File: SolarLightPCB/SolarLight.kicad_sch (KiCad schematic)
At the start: 18 parts, among them J1 I2C, J2 SPI, SW1 RotaryEncoder_Switch, U1 TP4056, U2 WeMos_D1_mini, U3 MCP1700-3302E

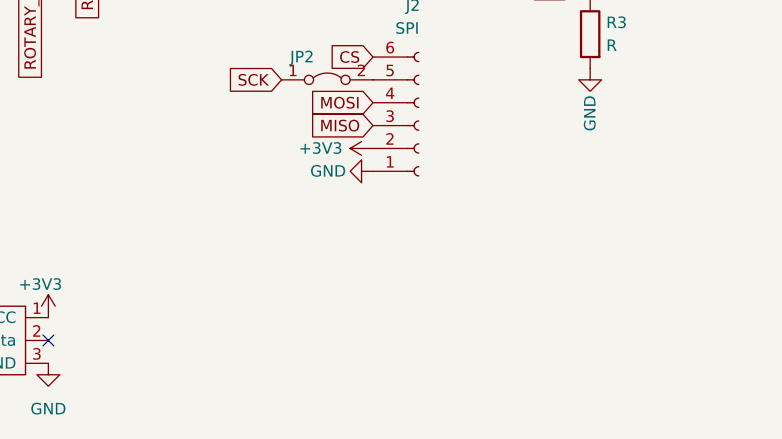
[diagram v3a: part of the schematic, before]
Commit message: Add GND Jumper
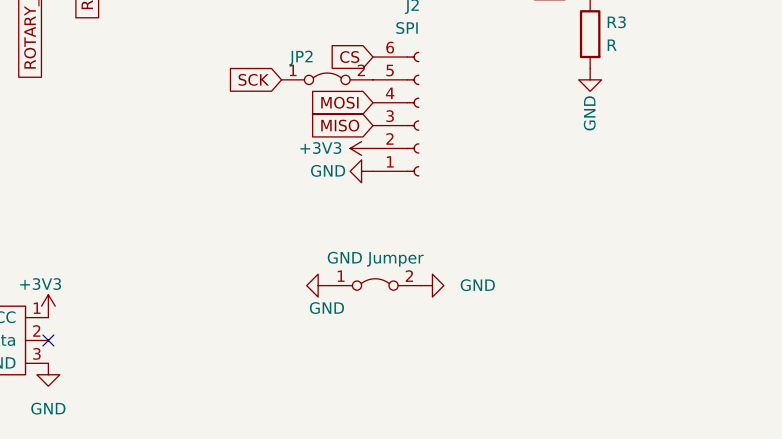
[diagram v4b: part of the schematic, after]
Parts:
- added JP6: GND Jumper, Resistor_THT:R_Axial_DIN0204_L3.6mm_D1.6mm_P5.08mm_Horizontal, symbol Jumper:Jumper_2_Bridged
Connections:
- net GND: now also JP6.1 (A), JP6.2 (B)
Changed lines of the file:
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@@
+    (pin "1")
+  )
+  (symbol (lib_id "power:GND") (at 185.42 130.048 270) (unit 1)
+    (in_bom yes) (on_board yes)
+    (property "Reference" "#PWR0121" (id 0) (at 179.07 130.048 0)
+      (effects (font (size 1.27 1.27)) hide)
+    )
+    (property "Value" "GND" (id 1) (at 183.134 132.588 90)
+      (effects (font (size 1.27 1.27)) (justify left))
+    )
+    (property "Footprint" "" (id 2) (at 185.42 130.048 0)
+      (effects (font (size 1.27 1.27)) hide)
+    )
+    (property "Datasheet" "" (id 3) (at 185.42 130.048 0)
+      (effects (font (size 1.27 1.27)) hide)
+    )
     (pin "1")
   )
@@
     (pin "6")
   )
+  (symbol (lib_id "Jumper:Jumper_2_Bridged") (at 190.5 130.048 0) (unit 1)
+    (in_bom yes) (on_board yes)
+    (property "Reference" "JP6" (id 0) (at 190.5 128.016 0)
+      (effects (font (size 1.27 1.27)) hide)
+    )
+    (property "Value" "GND Jumper" (id 1) (at 190.5 127 0))
+    (property "Footprint" "Resistor_THT:R_Axial_DIN0204_L3.6mm_D1.6mm_P5.08mm_Horizontal" (id 2) (at 190.5 130.048 0)
+      (effects (font (size 1.27 1.27)) hide)
+    )
+    (property "Datasheet" "~" (id 3) (at 190.5 130.048 0)
+      (effects (font (size 1.27 1.27)) hide)
+    )
+    (pin "1")
+    (pin "2")
+  )
   (symbol (lib_id "Jumper:SolderJumper_3_Bridged12") (at 152.146 90.424 270) (unit 1)
     (in_bom yes) (on_board yes) (fields_autoplaced)
@@
     )
     (property "Datasheet" "" (id 3) (at 197.866 63.246 0)
+      (effects (font (size 1.27 1.27)) hide)
+    )
+    (pin "1")
+  )
+  (symbol (lib_id "power:GND") (at 195.58 130.048 90) (unit 1)
+    (in_bom yes) (on_board yes) (fields_autoplaced)
+    (property "Reference" "#PWR0120" (id 0) (at 201.93 130.048 0)
+      (effects (font (size 1.27 1.27)) hide)
+    )
+    (property "Value" "GND" (id 1) (at 199.898 130.0479 90)
+      (effects (font (size 1.27 1.27)) (justify right))
+    )
+    (property "Footprint" "" (id 2) (at 195.58 130.048 0)
+      (effects (font (size 1.27 1.27)) hide)
+    )
+    (property "Datasheet" "" (id 3) (at 195.58 130.048 0)
       (effects (font (size 1.27 1.27)) hide)
     )
@@
       (reference "#PWR0119") (unit 1) (value "+3V3") (footprint "")
     )
+    (path "/8f53287b-acc6-4dbe-ac6e-98fe51c515c9"
+      (reference "#PWR0120") (unit 1) (value "GND") (footprint "")
+    )
+    (path "/053f9927-e4f2-4987-bb2c-996f494ab85a"
+      (reference "#PWR0121") (unit 1) (value "GND") (footprint "")
+    )
     (path "/1b639698-fdc2-412d-93eb-4fc53c894eea"
       (reference "BT1") (unit 1) (value "Battery_Cell") (footprint "Connector_PinHeader_2.54mm:PinHeader_1x02_P2.54mm_Vertical")
@@
       (reference "JP5") (unit 1) (value "POWER ON") (footprint "Connector_PinHeader_2.54mm:PinHeader_1x02_P2.54mm_Vertical")
     )
+    (path "/8628d11f-5b21-4013-8421-97343e641f3e"
+      (reference "JP6") (unit 1) (value "GND Jumper") (footprint "Resistor_THT:R_Axial_DIN0204_L3.6mm_D1.6mm_P5.08mm_Horizontal")
+    )
     (path "/efe1edb9-34c9-473f-839b-20e06ddf294c"

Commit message: Make a “simplified” version
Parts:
- removed J2: SPI, Connector_PinHeader_2.54mm:PinHeader_1x06_P2.54mm_Vertical, symbol Connector:Conn_01x06_Female
- removed JP1: Deep Sleep, Jumper:SolderJumper-2_P1.3mm_Bridged_Pad1.0x1.5mm, symbol Jumper:SolderJumper_2_Bridged
- removed JP2: Jumper_2_Bridged, Resistor_THT:R_Axial_DIN0204_L3.6mm_D1.6mm_P5.08mm_Horizontal, symbol Jumper:Jumper_2_Bridged
- removed JP3, JP4: SolderJumper_3_Bridged12, Jumper:SolderJumper-3_P1.3mm_Bridged12_Pad1.0x1.5mm, symbol Jumper:SolderJumper_3_Bridged12
- removed JP5: POWER ON, Connector_PinHeader_2.54mm:PinHeader_1x02_P2.54mm_Vertical, symbol Jumper:Jumper_2_Bridged
- removed JP6: GND Jumper, Resistor_THT:R_Axial_DIN0204_L3.6mm_D1.6mm_P5.08mm_Horizontal, symbol Jumper:Jumper_2_Bridged
- removed SW1: RotaryEncoder_Switch, Rotary_Encoder:RotaryEncoder_Alps_EC12E-Switch_Vertical_H20mm, symbol Device:RotaryEncoder_Switch
- added J2: Conn_01x06_Male, Connector_PinHeader_2.54mm:PinHeader_1x06_P2.54mm_Vertical, symbol Connector:Conn_01x06_Male
- added SW1: SW_Push, Button_Switch_THT:SW_PUSH_6mm_H4.3mm, symbol Switch:SW_Push
- BT1, SC1: footprint Connector_PinHeader_2.54mm:PinHeader_1x02_P2.54mm_Vertical -> TerminalBlock_Phoenix:TerminalBlock_Phoenix_PT-1,5-2-3.5-H_1x02_P3.50mm_Horizontal
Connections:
- net +3V3: now also J1.3 (Pin_3), U3.3 (VO), J2.2 (Pin_2); no longer J1.1 (Pin_1)
- net CS: now also J2.6 (Pin_6)
- net GND: now also J2.1 (Pin_1), SW1.2
- net MISO: now also J2.4 (Pin_4)
- net MOSI: now also J2.3 (Pin_3)
- net ROTARY_SWITCH: now also SW1.1
- net RST: now also U2.3 (D0)
- net SCK: now also J2.5 (Pin_5)
- net SCL: now also J1.1 (Pin_1), U2.14 (SCL/D1); no longer J1.2 (Pin_2)
- net SDA: now also J1.2 (Pin_2), U2.13 (SDA/D2); no longer J1.3 (Pin_3)
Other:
- moved on the sheet: BT1, J1, LIN1, LOUT1, U1, U2, U3

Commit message: Updated the simple pcb
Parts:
- added SW2: ON_OFF, Connector_PinHeader_2.54mm:PinHeader_1x03_P2.54mm_Vertical, symbol Switch:SW_SPST
- C1: footprint Capacitor_THT:CP_Radial_D5.0mm_P2.00mm -> Capacitor_THT:CP_Radial_D5.0mm_P2.50mm
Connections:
- net +3V3: now also SW2.2 (B); no longer LIN1.1 (VCC), LOUT1.1 (VCC), U3.3 (VO)
- net SCL: now also J1.2 (Pin_2); no longer J1.1 (Pin_1)
- net SDA: now also J1.1 (Pin_1); no longer J1.2 (Pin_2)
- net VOUT: now reaches U1.3 (OUT+), U3.2 (VI)
- net VOUT: now also LIN1.1 (VCC)
- new net: SW2.1 (A), U3.3 (VO)
- no-connect marks 4 -> 5
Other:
- moved on the sheet: C1
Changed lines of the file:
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@@
   )
   (no_connect (at 109.728 103.124))
+  (no_connect (at 83.312 100.584))
   (no_connect (at 153.67 96.52))
   (no_connect (at 146.05 114.3))
@@
     (stroke (width 0) (type default) (color 0 0 0 0))
   )
-  (global_label "SCL" (shape input) (at 190.5 77.47 180) (fields_autoplaced)
-    (effects (font (size 1.27 1.27)) (justify right))
-    (property "Intersheet References" "${INTERSHEET_REFS}" (id 0) (at 184.5793 77.3906 0)
+  (label "VOUT" (at 155.448 38.1 0)
+    (effects (font (size 1.27 1.27)) (justify left bottom))
+  )
+  (label "VOUT" (at 109.728 100.584 0)
+    (effects (font (size 1.27 1.27)) (justify left bottom))
+  )
+  (global_label "SCL" (shape input) (at 190.5 80.01 180) (fields_autoplaced)
+    (effects (font (size 1.27 1.27)) (justify right))
+    (property "Intersheet References" "${INTERSHEET_REFS}" (id 0) (at 184.5793 79.9306 0)
       (effects (font (size 1.27 1.27)) (justify right) hide)
     )
@@
     )
   )
-  (global_label "SDA" (shape input) (at 190.5 80.01 180) (fields_autoplaced)
-    (effects (font (size 1.27 1.27)) (justify right))
-    (property "Intersheet References" "${INTERSHEET_REFS}" (id 0) (at 184.5188 79.9306 0)
+  (global_label "SDA" (shape input) (at 190.5 77.47 180) (fields_autoplaced)
+    (effects (font (size 1.27 1.27)) (justify right))
+    (property "Intersheet References" "${INTERSHEET_REFS}" (id 0) (at 184.5188 77.3906 0)
       (effects (font (size 1.27 1.27)) (justify right) hide)
     )
@@
     (pin "1")
   )
-  (symbol (lib_id "power:+3V3") (at 109.728 100.584 0) (unit 1)
-    (in_bom yes) (on_board yes)
-    (property "Reference" "#PWR0106" (id 0) (at 109.728 104.394 0)
-      (effects (font (size 1.27 1.27)) hide)
-    )
-    (property "Value" "+3V3" (id 1) (at 108.839 96.901 0))
-    (property "Footprint" "" (id 2) (at 109.728 100.584 0)
-      (effects (font (size 1.27 1.27)) hide)
-    )
-    (property "Datasheet" "" (id 3) (at 109.728 100.584 0)
-      (effects (font (size 1.27 1.27)) hide)
-    )
-    (pin "1")
-  )
-  (symbol (lib_id "power:GND") (at 193.04 46.99 0) (unit 1)
-    (in_bom yes) (on_board yes) (fields_autoplaced)
-    (property "Reference" "#PWR0103" (id 0) (at 193.04 53.34 0)
-      (effects (font (size 1.27 1.27)) hide)
-    )
-    (property "Value" "GND" (id 1) (at 193.04 52.07 0))
-    (property "Footprint" "" (id 2) (at 193.04 46.99 0)
-      (effects (font (size 1.27 1.27)) hide)
-    )
-    (property "Datasheet" "" (id 3) (at 193.04 46.99 0)
+  (symbol (lib_id "power:GND") (at 199.898 44.958 0) (unit 1)
+    (in_bom yes) (on_board yes) (fields_autoplaced)
+    (property "Reference" "#PWR0103" (id 0) (at 199.898 51.308 0)
+      (effects (font (size 1.27 1.27)) hide)
+    )
+    (property "Value" "GND" (id 1) (at 199.898 50.038 0))
+    (property "Footprint" "" (id 2) (at 199.898 44.958 0)
+      (effects (font (size 1.27 1.27)) hide)
+    )
+    (property "Datasheet" "" (id 3) (at 199.898 44.958 0)
       (effects (font (size 1.27 1.27)) hide)
     )
@@
     (pin "1")
   )
-  (symbol (lib_id "power:+3V3") (at 179.07 38.1 0) (unit 1)
-    (in_bom yes) (on_board yes)
-    (property "Reference" "#PWR0104" (id 0) (at 179.07 41.91 0)
-      (effects (font (size 1.27 1.27)) hide)
-    )
-    (property "Value" "+3V3" (id 1) (at 179.578 32.258 0))
-    (property "Footprint" "" (id 2) (at 179.07 38.1 0)
-      (effects (font (size 1.27 1.27)) hide)
-    )
-    (property "Datasheet" "" (id 3) (at 179.07 38.1 0)
+  (symbol (lib_id "power:+3V3") (at 189.23 38.1 0) (unit 1)
+    (in_bom yes) (on_board yes)
+    (property "Reference" "#PWR0104" (id 0) (at 189.23 41.91 0)
+      (effects (font (size 1.27 1.27)) hide)
+    )
+    (property "Value" "+3V3" (id 1) (at 189.738 32.258 0))
+    (property "Footprint" "" (id 2) (at 189.23 38.1 0)
+      (effects (font (size 1.27 1.27)) hide)
+    )
+    (property "Datasheet" "" (id 3) (at 189.23 38.1 0)
       (effects (font (size 1.27 1.27)) hide)
     )
@@
     (pin "1")
   )
-  (symbol (lib_id "power:+3V3") (at 193.04 39.37 0) (unit 1)
-    (in_bom yes) (on_board yes) (fields_autoplaced)
-    (property "Reference" "#PWR0105" (id 0) (at 193.04 43.18 0)
-      (effects (font (size 1.27 1.27)) hide)
-    )
-    (property "Value" "+3V3" (id 1) (at 193.04 34.29 0))
-    (property "Footprint" "" (id 2) (at 193.04 39.37 0)
-      (effects (font (size 1.27 1.27)) hide)
-    )
-    (property "Datasheet" "" (id 3) (at 193.04 39.37 0)
+  (symbol (lib_id "power:+3V3") (at 199.898 37.338 0) (unit 1)
+    (in_bom yes) (on_board yes) (fields_autoplaced)
+    (property "Reference" "#PWR0105" (id 0) (at 199.898 41.148 0)
+      (effects (font (size 1.27 1.27)) hide)
+    )
+    (property "Value" "+3V3" (id 1) (at 199.898 32.258 0))
+    (property "Footprint" "" (id 2) (at 199.898 37.338 0)
+      (effects (font (size 1.27 1.27)) hide)
+    )
+    (property "Datasheet" "" (id 3) (at 199.898 37.338 0)
       (effects (font (size 1.27 1.27)) hide)
     )
@@
     )
     (pin "1")
+  )
+  (symbol (lib_id "Switch:SW_SPST") (at 184.15 38.1 0) (unit 1)
+    (in_bom yes) (on_board yes)
+    (property "Reference" "SW2" (id 0) (at 184.15 40.64 0))
+    (property "Value" "ON_OFF" (id 1) (at 184.658 34.798 0))
+    (property "Footprint" "Connector_PinHeader_2.54mm:PinHeader_1x03_P2.54mm_Vertical" (id 2) (at 184.15 38.1 0)
+      (effects (font (size 1.27 1.27)) hide)
+    )
+    (property "Datasheet" "~" (id 3) (at 184.15 38.1 0)
+      (effects (font (size 1.27 1.27)) hide)
+    )
+    (pin "1")
+    (pin "2")
   )
   (symbol (lib_id "Connector:Conn_01x04_Female") (at 195.58 80.01 0) (unit 1)
@@
     (pin "9")
   )
-  (symbol (lib_id "power:+3V3") (at 83.312 100.584 0) (unit 1)
-    (in_bom yes) (on_board yes)
-    (property "Reference" "#PWR0113" (id 0) (at 83.312 104.394 0)
-      (effects (font (size 1.27 1.27)) hide)
-    )
-    (property "Value" "+3V3" (id 1) (at 82.423 96.901 0))
-    (property "Footprint" "" (id 2) (at 83.312 100.584 0)
-      (effects (font (size 1.27 1.27)) hide)
-    )
-    (property "Datasheet" "" (id 3) (at 83.312 100.584 0)
-      (effects (font (size 1.27 1.27)) hide)
-    )
-    (pin "1")
-  )
   (symbol (lib_id "Device:R") (at 214.376 91.694 0) (unit 1)
     (in_bom yes) (on_board yes) (fields_autoplaced)
@@
     (pin "3")
   )
-  (symbol (lib_id "Device:C_Polarized") (at 193.04 43.18 0) (unit 1)
-    (in_bom yes) (on_board yes)
-    (property "Reference" "C1" (id 0) (at 197.358 43.18 0)
-      (effects (font (size 1.27 1.27)) (justify left))
-    )
-    (property "Value" "C_Polarized" (id 1) (at 196.85 43.5609 0)
-      (effects (font (size 1.27 1.27)) (justify left) hide)
-    )
-    (property "Footprint" "Capacitor_THT:CP_Radial_D5.0mm_P2.00mm" (id 2) (at 194.0052 46.99 0)
-      (effects (font (size 1.27 1.27)) hide)
-    )
-    (property "Datasheet" "~" (id 3) (at 193.04 43.18 0)
+  (symbol (lib_id "Device:C_Polarized") (at 199.898 41.148 0) (unit 1)
+    (in_bom yes) (on_board yes)
+    (property "Reference" "C1" (id 0) (at 204.216 41.148 0)
+      (effects (font (size 1.27 1.27)) (justify left))
+    )
+    (property "Value" "C_Polarized" (id 1) (at 203.708 41.5289 0)
+      (effects (font (size 1.27 1.27)) (justify left) hide)
+    )
+    (property "Footprint" "Capacitor_THT:CP_Radial_D5.0mm_P2.50mm" (id 2) (at 200.8632 44.958 0)
+      (effects (font (size 1.27 1.27)) hide)
+    )
+    (property "Datasheet" "~" (id 3) (at 199.898 41.148 0)
       (effects (font (size 1.27 1.27)) hide)
     )
@@
       (reference "#PWR0105") (unit 1) (value "+3V3") (footprint "")
     )
-    (path "/2c65fd9b-6b86-4de9-88d8-fcb1dcaf593d"
-      (reference "#PWR0106") (unit 1) (value "+3V3") (footprint "")
-    )
     (path "/e78c0649-b4a3-4f91-ac29-c9de53c1e159"
       (reference "#PWR0107") (unit 1) (value "+3V3") (footprint "")
@@
       (reference "#PWR0112") (unit 1) (value "GND") (footprint "")
     )
-    (path "/d59a7dd3-39c1-4aa7-a4e7-bbb3a867df2f"
-      (reference "#PWR0113") (unit 1) (value "+3V3") (footprint "")
-    )
     (path "/61e0ffe0-75fe-4e05-9458-0e51d8f81bec"
       (reference "#PWR0114") (unit 1) (value "GND") (footprint "")
@@
     )
     (path "/e60a1f34-6b2f-498f-916b-89bff7055f25"
-      (reference "C1") (unit 1) (value "C_Polarized") (footprint "Capacitor_THT:CP_Radial_D5.0mm_P2.00mm")
+      (reference "C1") (unit 1) (value "C_Polarized") (footprint "Capacitor_THT:CP_Radial_D5.0mm_P2.50mm")
     )
     (path "/b014f64b-63d7-4679-a15c-8f4cf024b19d"
@@
       (reference "SW1") (unit 1) (value "SW_Push") (footprint "Button_Switch_THT:SW_PUSH_6mm_H4.3mm")
     )
+    (path "/9f6d55fb-712b-4d9f-992e-0229120b6895"
+      (reference "SW2") (unit 1) (value "ON_OFF") (footprint "Connector_PinHeader_2.54mm:PinHeader_1x03_P2.54mm_Vertical")
+    )
     (path "/7a9b99af-c42f-4684-b0b2-ed8a4e18f952"
